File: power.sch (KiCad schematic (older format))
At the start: 40 parts, among them U1 TPS54325, U2 TPS54294

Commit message: Add ferrite bead footprints
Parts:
- FB1, FB?: footprint (none) -> Local:BLM21AG102SN1D
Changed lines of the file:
@@
 F 0 "FB1" V 9876 4600 50  0000 C CNN
 F 1 "Ferrite_Bead" V 9967 4600 50  0000 C CNN
-F 2 "" V 10080 4600 50  0001 C CNN
+F 2 "Local:BLM21AG102SN1D" V 10080 4600 50  0001 C CNN
 F 3 "~" H 10150 4600 50  0001 C CNN
 	1    10150 4600
@@
 F 0 "FB?" V 3276 6800 50  0000 C CNN
 F 1 "Ferrite_Bead" V 3367 6800 50  0000 C CNN
-F 2 "" V 3480 6800 50  0001 C CNN
+F 2 "Local:BLM21AG102SN1D" V 3480 6800 50  0001 C CNN
 F 3 "~" H 3550 6800 50  0001 C CNN
 	1    3550 6800

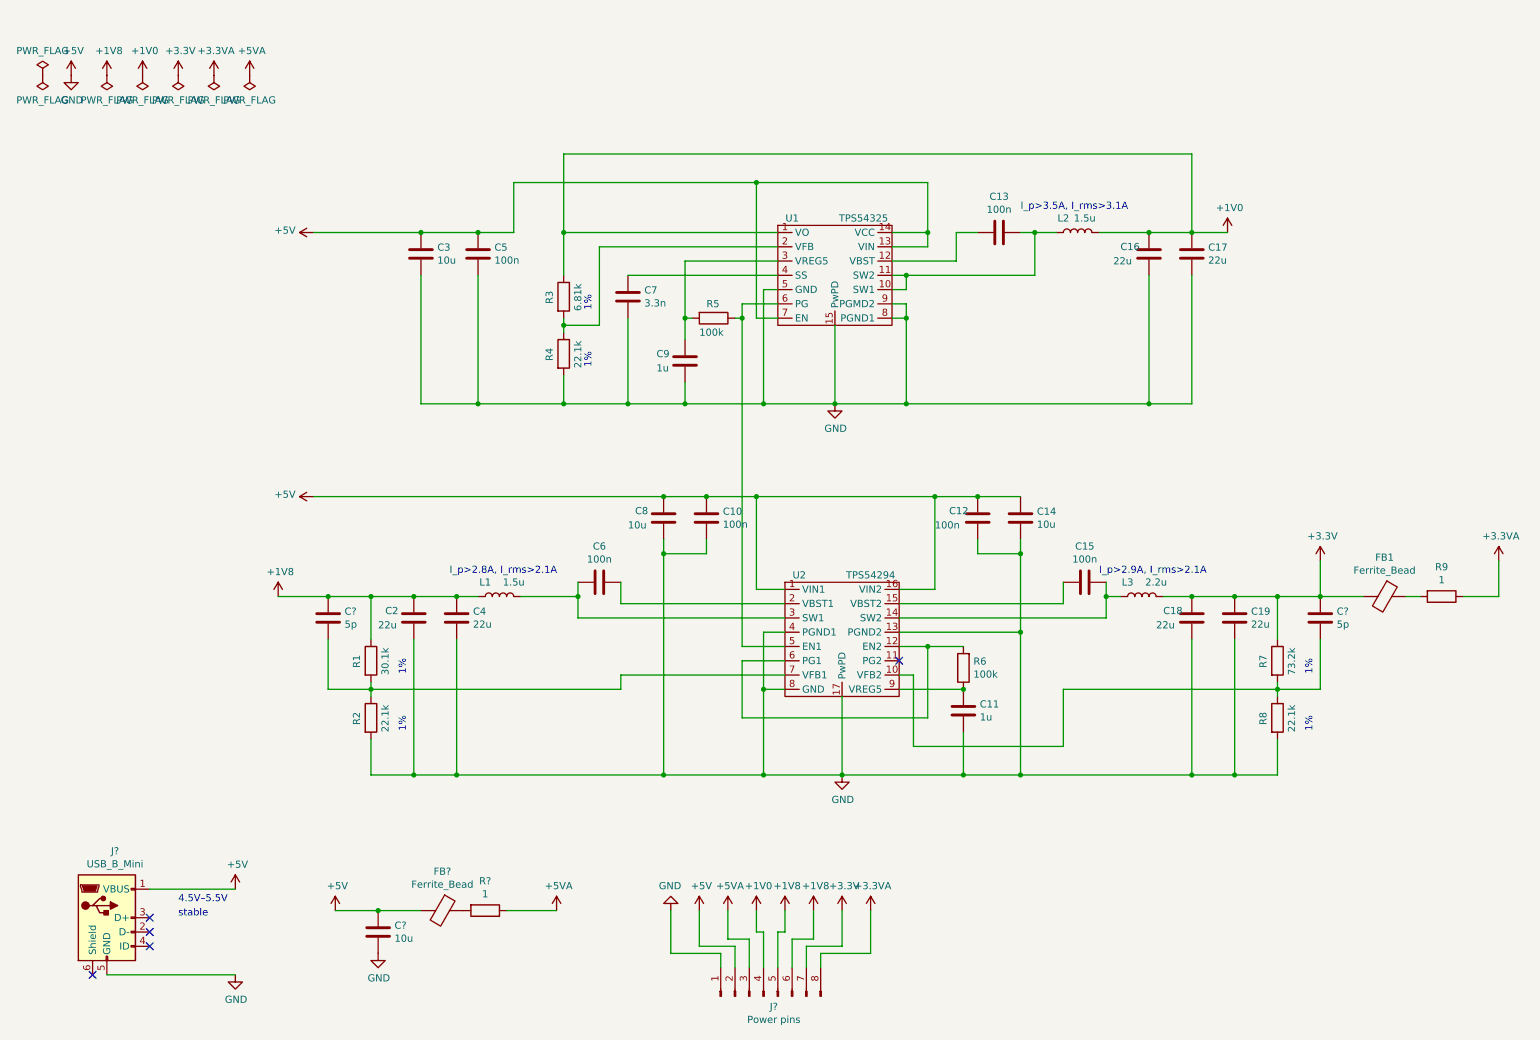
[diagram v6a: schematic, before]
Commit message: Remove USB jack, add power jack
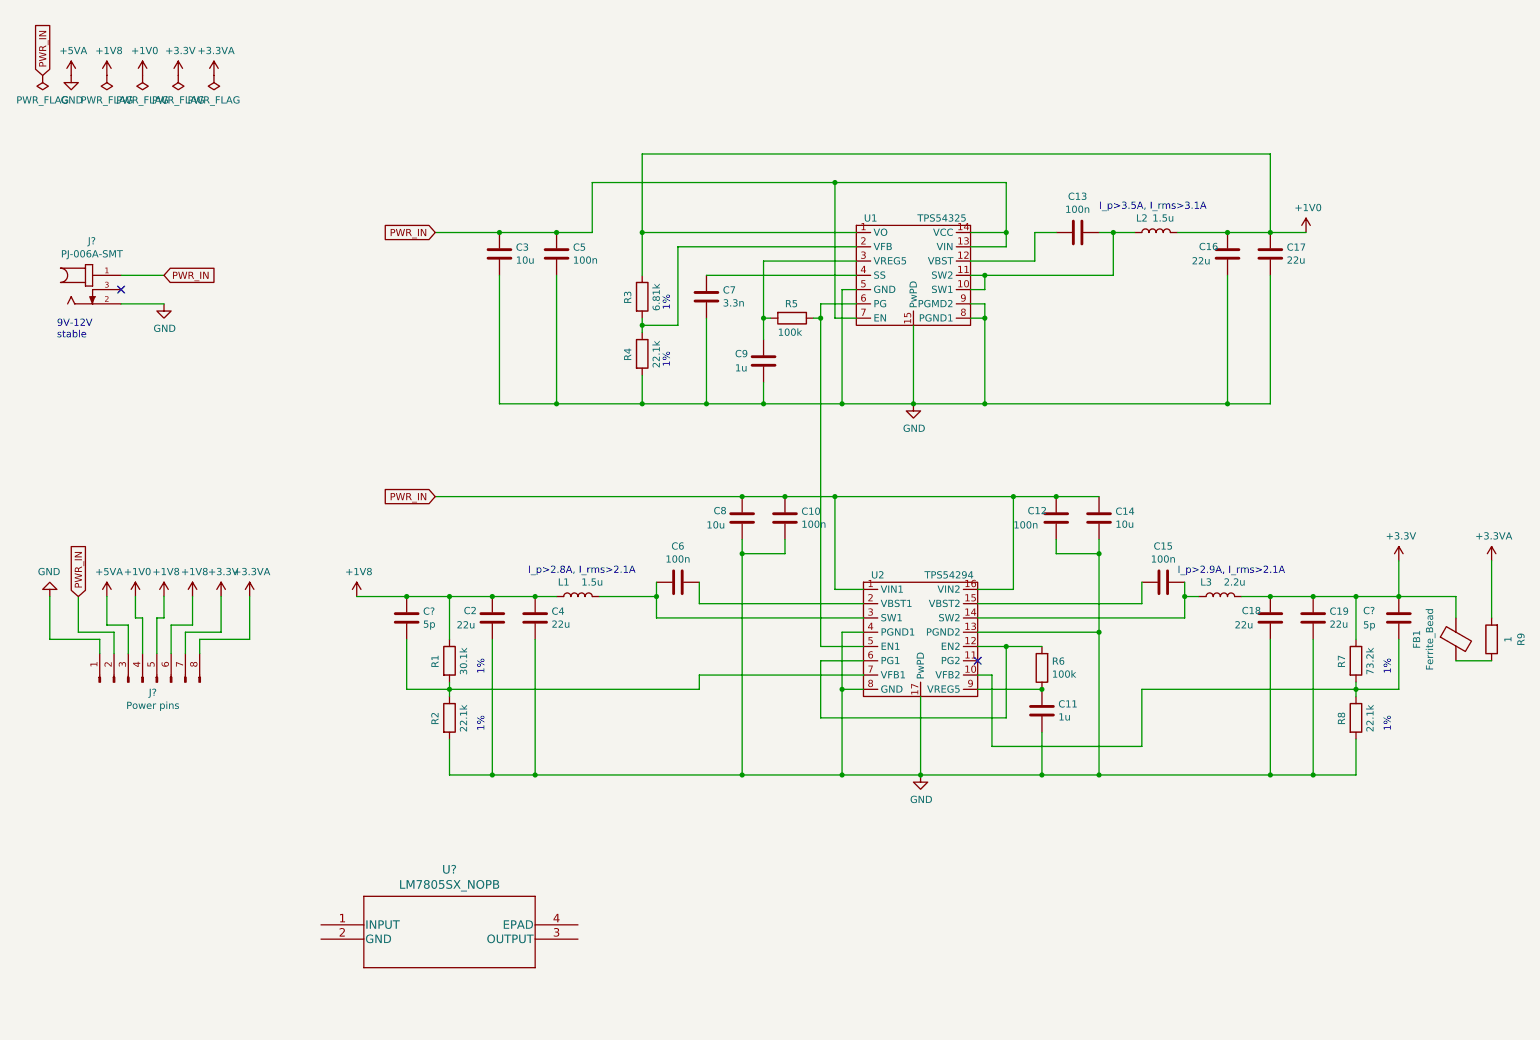
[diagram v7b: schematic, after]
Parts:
- removed C?: 10u, symbol Device:C
- removed FB?: Ferrite_Bead, Local:BLM21AG102SN1D, symbol Device:Ferrite_Bead
- removed J?: USB_B_Mini, Local:USB_Mini_B_Female_690-005-299-043, symbol Connector:USB_B_Mini
- removed R?: 1, symbol Device:R
- added J?: PJ-006A-SMT, PJ-006A-SMT:CUI_PJ-006A-SMT, symbol PJ-006A-SMT:PJ-006A-SMT
- added U?: LM7805SX_NOPB, Local:LM7805SX&slash_NOPB, symbol lm7805:LM7805SX_NOPB
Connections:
- net +3.3VA: now also R9.2; no longer R9.1
- net +3V3: now also FB1.1; no longer FB1.2
- net +5VA: now also C10.2, C11.2, C12.2, C14.2, C16.2, C17.2, C18.2, C19.2, C2.2, C3.2, C4.2, C5.2, C7.2, C8.2, C9.2, J?.1 (Pin_1), R2.2, R4.2, R8.2, U1.15 (PwPD), U1.5 (GND), U1.8 (PGND1), U1.9 (PGMD2), U2.13 (PGND2), U2.17 (PwPD), U2.4 (PGND1), U2.8 (GND), J?.2
- removed net +5V: C10.1, C10.2, C11.2, C12.1, C12.2, C14.1, C14.2, C16.2, C17.2, C18.2, C19.2, C2.2, C3.1, C3.2, C4.2, C5.1, C5.2, C7.2, C8.1, C8.2, C9.2, J?.1 (Pin_1), J?.2 (Pin_2), R2.2, R4.2, R8.2, U1.13 (VIN), U1.14 (VCC), U1.15 (PwPD), U1.5 (GND), U1.7 (EN), U1.8 (PGND1), U1.9 (PGMD2), U2.1 (VIN1), U2.13 (PGND2), U2.16 (VIN2), U2.17 (PwPD), U2.4 (PGND1), U2.8 (GND)
- new net: FB1.2, R9.1
- new net PWR_IN: C10.1, C12.1, C14.1, C3.1, C5.1, C8.1, J?.1, J?.2 (Pin_2), U1.13 (VIN), U1.14 (VCC), U1.7 (EN), U2.1 (VIN1), U2.16 (VIN2)
- no-connect marks 5 -> 2
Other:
- note added: "9V-12V\nstable"
- note removed: "4.5V–5.5V"
- note removed: "stable"
- moved on the sheet: C10, C11, C12, C13, C14, C15, C16, C17, C18, C19, C2, C3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

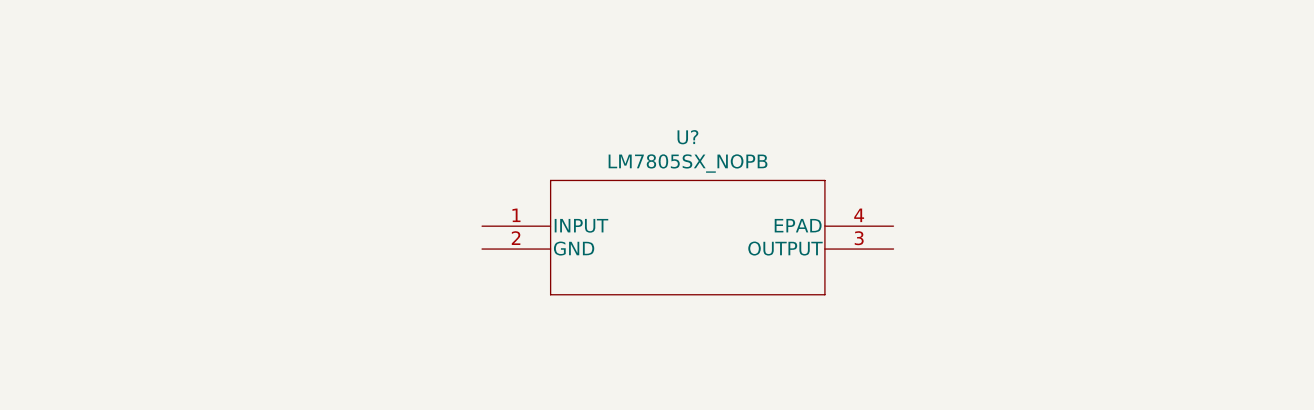
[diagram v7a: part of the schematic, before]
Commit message: Wire 5V vreg
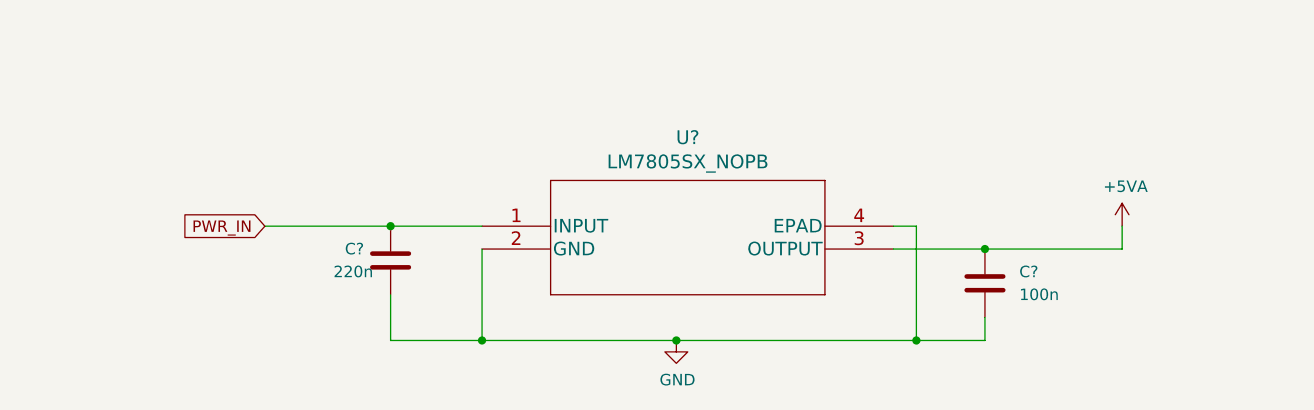
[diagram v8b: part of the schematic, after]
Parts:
- added C?: 220n, symbol Device:C
- added C?: 100n, symbol Device:C
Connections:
- net +5VA: now also U?.2 (GND), U?.3 (OUTPUT), U?.4 (EPAD), C?.1, C?.2, C?.2
- net PWR_IN: now also U?.1 (INPUT), C?.1
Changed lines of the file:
@@
 $EndComp
 NoConn ~ 1300 2450
+$Comp
+L Device:C C?
+U 1 1 5D917080
+P 2300 7050
+F 0 "C?" H 2100 7100 50  0000 L CNN
+F 1 "220n" H 2050 7000 50  0000 L CNN
+F 2 "" H 2338 6900 50  0001 C CNN
+F 3 "~" H 2300 7050 50  0001 C CNN
+	1    2300 7050
+	1    0    0    -1
+$EndComp
+$Comp
+L Device:C C?
+U 1 1 5D91829A
+P 4900 7150
+F 0 "C?" H 5050 7200 50  0000 L CNN
+F 1 "100n" H 5050 7100 50  0000 L CNN
+F 2 "" H 4938 7000 50  0001 C CNN
+F 3 "~" H 4900 7150 50  0001 C CNN
+	1    4900 7150
+	1    0    0    -1
+$EndComp
+Text GLabel 1750 6900 0    50   Input ~ 0
+PWR_IN
+$Comp
+L power:GND #PWR?
+U 1 1 5D918F8E
+P 3550 7400
+F 0 "#PWR?" H 3550 7150 50  0001 C CNN
+F 1 "GND" H 3555 7227 50  0000 C CNN
+F 2 "" H 3550 7400 50  0001 C CNN
+F 3 "" H 3550 7400 50  0001 C CNN
+	1    3550 7400
+	1    0    0    -1
+$EndComp
+Wire Wire Line
+	4900 7400 4600 7400
+Wire Wire Line
+	2700 7000 2700 7400
+Wire Wire Line
+	2700 7400 3550 7400
+Connection ~ 3550 7400
+Wire Wire Line
+	2300 7200 2300 7400
+Wire Wire Line
+	2300 7400 2700 7400
+Connection ~ 2700 7400
+Wire Wire Line
+	1750 6900 2300 6900
+Connection ~ 2300 6900
+Wire Wire Line
+	2300 6900 2700 6900
+$Comp
+L power:+5VA #PWR?
+U 1 1 5D94A231
+P 5500 6900
+F 0 "#PWR?" H 5500 6750 50  0001 C CNN
+F 1 "+5VA" H 5515 7073 50  0000 C CNN
+F 2 "" H 5500 6900 50  0001 C CNN
+F 3 "" H 5500 6900 50  0001 C CNN
+	1    5500 6900
+	1    0    0    -1
+$EndComp
+Wire Wire Line
+	4900 7400 4900 7300
+Wire Wire Line
+	4500 7000 4900 7000
+Wire Wire Line
+	4900 7000 5500 7000
+Wire Wire Line
+	5500 7000 5500 6900
+Connection ~ 4900 7000
+Wire Wire Line
+	4500 6900 4600 6900
+Wire Wire Line
+	4600 6900 4600 7400
+Connection ~ 4600 7400
+Wire Wire Line
+	4600 7400 3550 7400
 $EndSCHEMATC
